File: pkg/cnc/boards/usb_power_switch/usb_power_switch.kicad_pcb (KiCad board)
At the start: 2 copper layers, 15.7 x 22.8 mm, 14 parts, among them J1 USB_A_FEMALE, J2 USB_A_MALE, J3 EN, Q1 DMG2301L

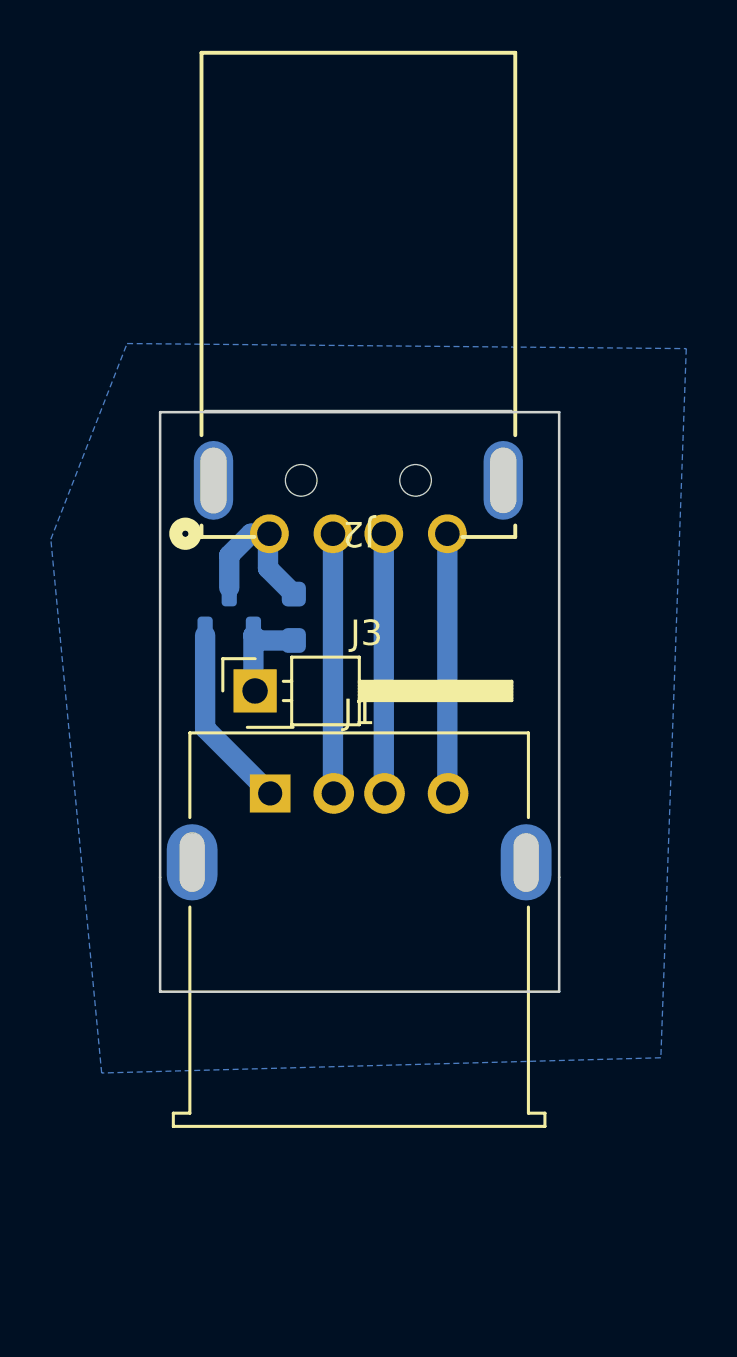
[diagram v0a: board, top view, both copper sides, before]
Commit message: Add PCB CAM and Voron toolboard stuff.
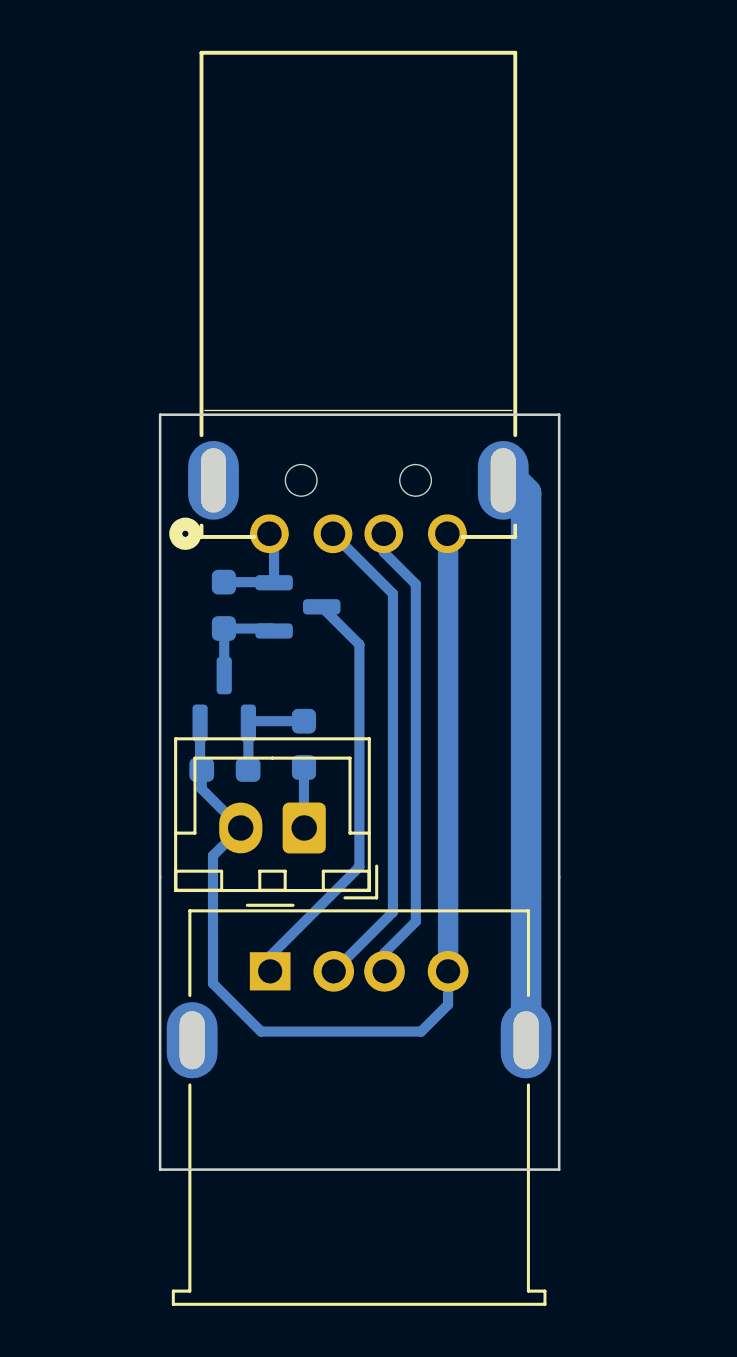
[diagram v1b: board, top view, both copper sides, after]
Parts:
- removed ? (x9): , 
- added Q2: 2N7002, Package_TO_SOT_SMD:SOT-23, B.Cu at (109.0, 74.5)
- added R2: 100K, Resistor_SMD:R_0603_1608Metric_Pad0.98x0.95mm_HandSolder, B.Cu at (109.0, 77.3)
- added R3: 50K, Resistor_SMD:R_0603_1608Metric_Pad0.98x0.95mm_HandSolder, B.Cu at (112.2, 76.3)
- J3: value EN -> Conn_01x02; footprint Connector_PinHeader_2.54mm:PinHeader_1x01_P2.54mm_Horizontal -> Connector_JST:JST_XH_B2B-XH-A_1x02_P2.50mm_Vertical
- moved J1 7.00 mm to (110.8, 85.2)
- moved J3 5.73 mm to (112.2, 79.6), turned to 180 degrees
- moved R1 2.79 mm to (109.0, 70.8)
- moved Q1 2.71 mm to (111.9, 70.9), turned to 0 degrees
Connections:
- net Net-(J1-D+) renamed D+
- net Net-(J1-D-) renamed D-
- Q1 pad 1: Net-(J3-Pin_1) -> Net-(Q1-G)
- Q1 pad 2: 5V_OUT -> +5V
- Q1 pad 3: +5V -> 5V_OUT
- R1 pad 2: Net-(J3-Pin_1) -> Net-(Q1-G)
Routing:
- net GND: track 10.3 -> 40.4 mm
- net SHIELD: track 0.00 -> 22.2 mm
- net 5V_OUT: track 7.28 -> 16.4 mm
- net D-: track 10.3 -> 19.2 mm
- net D+: track 10.2 -> 18.2 mm
- net Net-(Q2-G): track 0.00 -> 4.06 mm
- net Net-(Q1-G): track 0.00 -> 3.87 mm
- net +5V: track 6.56 -> 3.98 mm
- net Net-(J3-Pin_1): track 3.89 -> 2.38 mm
- removed copper zone on B.Cu, net SHIELD
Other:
- board size 15.7 x 22.8 mm -> 15.7 x 29.7 mm
